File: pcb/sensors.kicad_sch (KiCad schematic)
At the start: 17 parts, among them IC7 SHT20, Q2 TEMT6000X01, U4 LMV321

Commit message: created step file
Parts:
- removed C21, C28, C8: 100n, Capacitor_SMD:C_0402_1005Metric, symbol Capacitor_JLC:100n
- removed C25: 4.7u, Capacitor_SMD:C_1206_3216Metric, symbol Capacitor_JLC:4.7u
- removed C26: 1u, Capacitor_SMD:C_0402_1005Metric, symbol Capacitor_JLC:1u
- removed C27: 27p, Capacitor_SMD:C_0402_1005Metric, symbol Capacitor_JLC:27p
- removed IC7: SHT20, SON100P300X300X110-7N, symbol Sensors_JLC:SHT20
- removed MK1: AP2718AT, AP2718AT, symbol Misc_JLC:AP2718AT
- removed R1, R2, R31: 4.7k, Resistor_SMD:R_0402_1005Metric, symbol Resistor_JLC:4.7k
- removed R32, R33: 10k, Resistor_SMD:R_0402_1005Metric, symbol Resistor_JLC:10k
- removed R34: 300k, Resistor_SMD:R_0402_1005Metric, symbol Resistor_JLC:300k
- removed U4: LMV321, Package_TO_SOT_SMD:SOT-23-5, symbol Amplifier_JLC:LMV321
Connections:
- net LIGHT_MIC_PWR renamed LIGHT_PWR
- no-connect marks 2 -> 0
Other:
- note removed: "MICROPHONE"
- note removed: "PULL UP RESISTORS"
- note removed: "SHT-20"
- moved on the sheet: Q2, R35

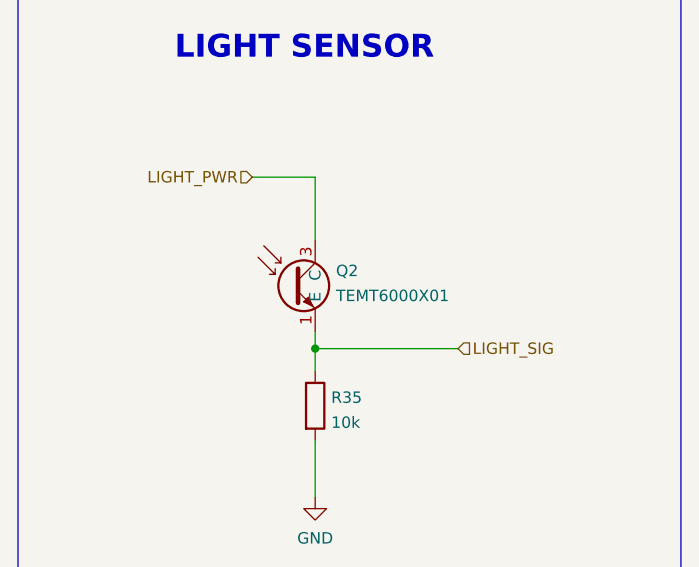
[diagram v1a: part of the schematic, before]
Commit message: Added demo scripts
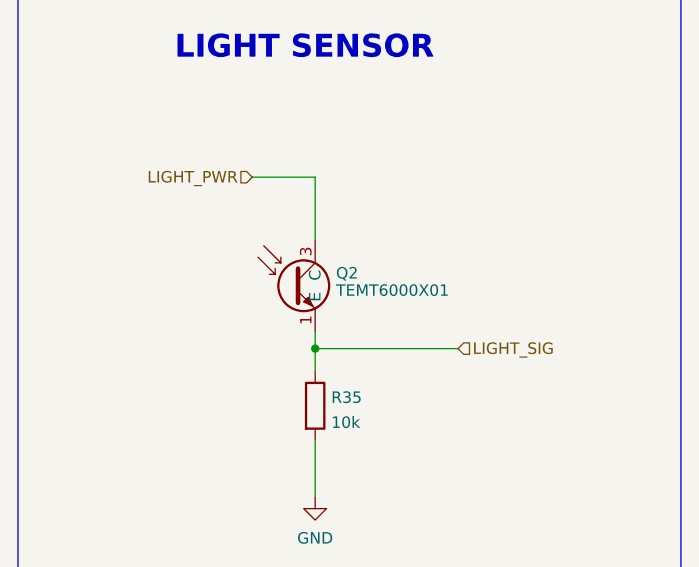
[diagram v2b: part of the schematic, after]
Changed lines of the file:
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@@
   (symbol (lib_id "Transistor_JLC:TEMT6000X01") (at 186.055 151.765 0) (unit 1)
     (in_bom yes) (on_board yes) (dnp no) (fields_autoplaced)
-    (property "Reference" "Q2" (at 188.3664 145.0272 0)
+    (property "Reference" "Q2" (at 188.3664 145.292 0)
       (effects (font (size 1.27 1.27)) (justify left))
     )
-    (property "Value" "TEMT6000X01" (at 188.3664 147.8023 0)
+    (property "Value" "TEMT6000X01" (at 188.3664 147.213 0)
       (effects (font (size 1.27 1.27)) (justify left))
     )

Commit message: Completed initial schematic
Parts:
- added C12, C3, C5: 100n, Capacitor_SMD:C_0402_1005Metric, symbol Capacitor_JLC:100n
- added C2: 470p, Capacitor_SMD:C_0603_1608Metric, symbol Capacitor_JLC:470p
- added C4: 10n, Capacitor_SMD:C_0402_1005Metric, symbol Capacitor_JLC:10n
- added C6: 4.7u, Capacitor_SMD:C_1206_3216Metric, symbol Capacitor_JLC:4.7u
- added D1: 1N4148WS, Diode_SMD:D_SOD-323F, symbol Diode_JLC:1N4148WS
- added IC1: NE555DR, SOIC127P600X175-8N, symbol Misc_JLC:NE555DR
- added IC2: LM358DR2G, SOIC127P600X175-8N, symbol Power-Drivers_JLC:LM358DR2G
- added IC4: AHT20, AHT20, symbol Sensors_JLC:AHT20
- added R3: 1.5k, Resistor_SMD:R_0402_1005Metric, symbol Resistor_JLC:1.5k
- added R4: 2.4k, Resistor_SMD:R_0402_1005Metric, symbol Resistor_JLC:2.4k
- added R5: 10k, Resistor_SMD:R_0402_1005Metric, symbol Resistor_JLC:10k
- added R6: 1M, Resistor_SMD:R_0402_1005Metric, symbol Resistor_JLC:1M
- added R9: 100, Resistor_SMD:R_0402_1005Metric, symbol Resistor_JLC:100
- added TP4: TestPoint_Alt, TestPoint:TestPoint_Pad_1.0x1.0mm, symbol personal:TestPoint_Alt
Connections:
- net GND: now also C12.2, C2.2, C3.2, C4.2, C5.2, C6.2, IC1.1 (GND), IC2.4 (VEE/GND), IC2.5 (INPUTB-POS), IC2.6 (INPUTB-NEG), IC2.7 (OUTPUTB), IC4.5 (GND), R6.2
- new net: D1.2 (A), R5.1
- new net: IC2.1 (OUTPUTA), IC2.2 (INPUTA-NEG), R9.1
- new net: IC1.3 (OUT), R5.2
- new net: C2.1, IC1.2 (TRIG), IC1.6 (THRES), R4.2
- new net: C4.1, IC1.5 (CONT)
- new net: IC1.7 (DISCH), R3.2, R4.1
- new net +3V3: C12.1, C3.1, C5.1, IC1.4 (~{RESET}), IC1.8 (VCC), IC2.8 (VCC), IC4.2 (VDD), R3.1
- new net CAP_SIG: C6.1, R9.2
- new net I2C_SCL: IC4.3 (SCL)
- new net I2C_SDA: IC4.4 (SDA)
- new net SIG_RAW: D1.1 (K), IC2.3 (INPUTA-POS), R6.1, TP4.1
- no-connect marks 0 -> 2
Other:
- note added: "CAP MOISTURE SENSOR"
- moved on the sheet: Q2, R35

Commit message: updated design
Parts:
- removed TP4: TestPoint_Alt, TestPoint:TestPoint_Pad_1.0x1.0mm, symbol personal:TestPoint_Alt
- added C19: 100n, Capacitor_SMD:C_0402_1005Metric, symbol Capacitor_JLC:100n
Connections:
- net +3V3: now also C19.1
- net GND: now also C19.2
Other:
- note added: "ENVIRONMENTAL SENSOR"
- moved on the sheet: Q2

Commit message: created fab files
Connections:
- net LIGHT_PWR is gone; now on net I2C_PWR: Q2.3 (C)
- net +3V3 renamed I2C_PWR
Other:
- note added: "PERIPHERAL POWER"
